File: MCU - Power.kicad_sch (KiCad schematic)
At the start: 29 parts, among them J3 B2B-PH-K-S, U1 STM32H743ZIT6TR

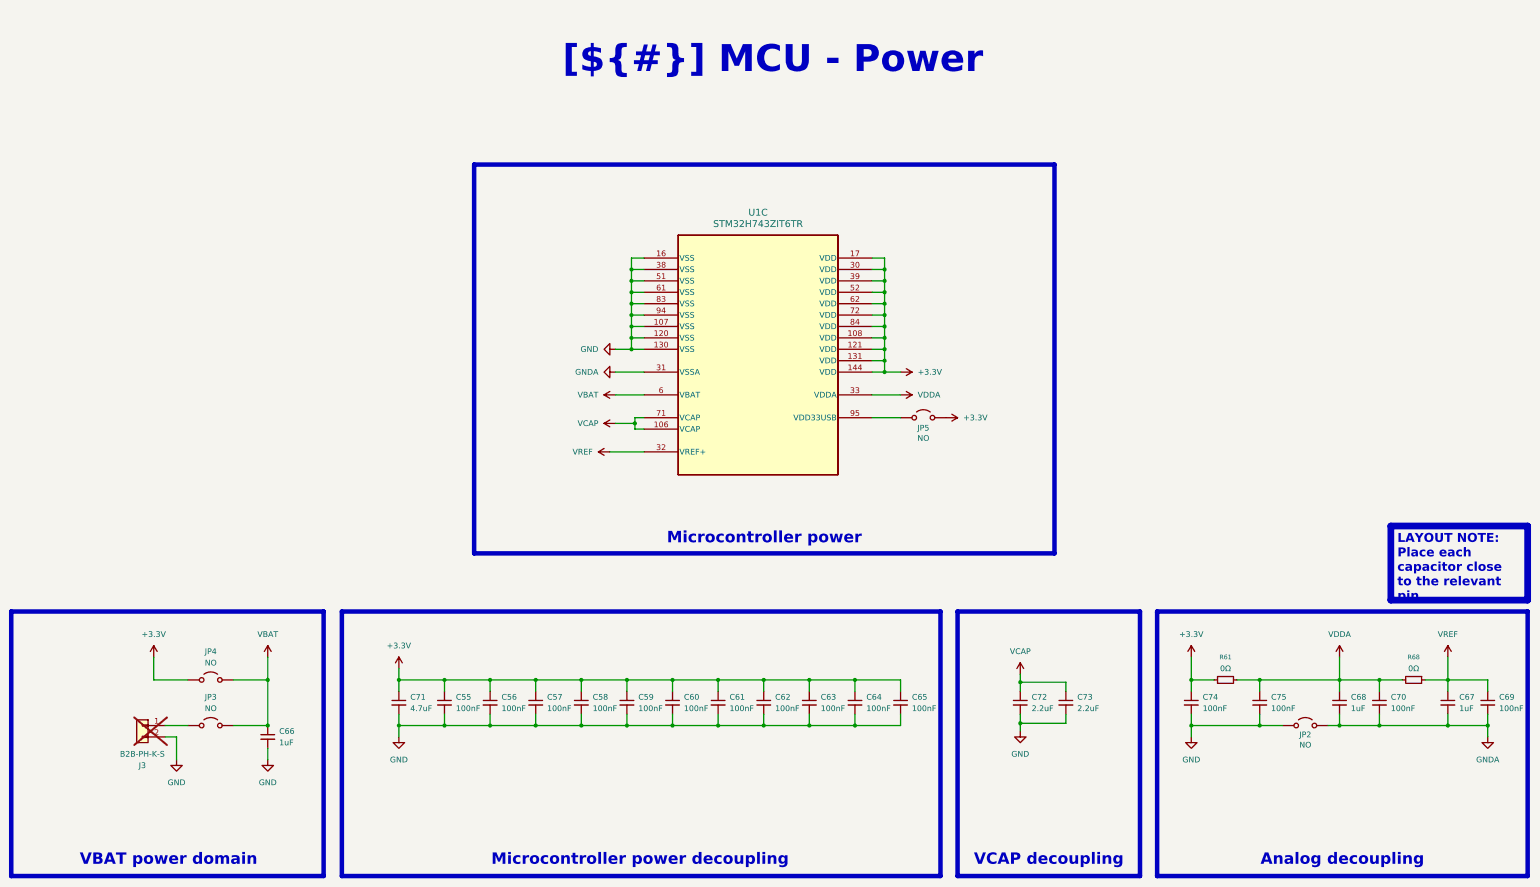
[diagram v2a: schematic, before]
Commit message: change some solder bridges from no to nc
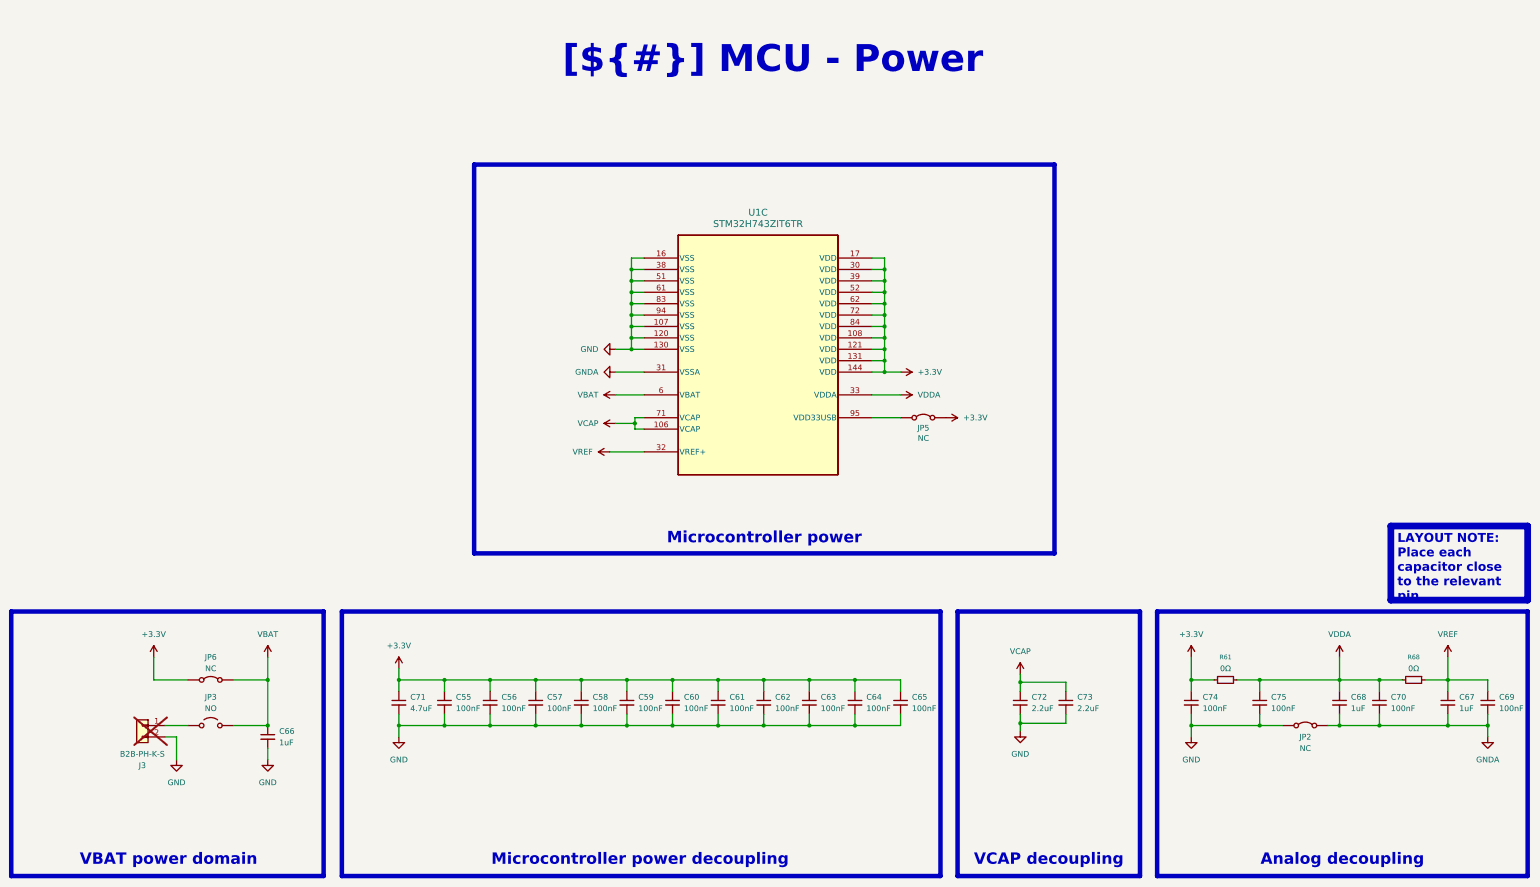
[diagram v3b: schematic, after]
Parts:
- removed JP2, JP4, JP5: NO, Jumper:SolderJumper-2_P1.3mm_Open_TrianglePad1.0x1.5mm, symbol 0_modules:Jumper_2_Open
- added JP2, JP5, JP6: NC, Jumper:SolderJumper-2_P1.3mm_Open_TrianglePad1.0x1.5mm, symbol 0_modules:Jumper_2_Bridged
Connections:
- net +3.3V: now also JP5.2 (B), JP6.1 (A)
- net GND: now also JP2.1 (A)
- net GNDA: now also JP2.2 (B)
- net VBAT: now also JP6.2 (B)
- net at U1.95 (VDD33USB): now also JP5.1 (A)
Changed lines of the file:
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@@
+	)
+	(symbol
+		(lib_id "0_modules:Jumper_2_Bridged")
+		(at 328.93 170.18 0)
+		(unit 1)
+		(exclude_from_sim no)
+		(in_bom yes)
+		(on_board yes)
+		(dnp no)
+		(property "Reference" "JP2"
+			(at 328.93 172.72 0)
+			(effects
+				(font
+					(size 1.27 1.27)
+				)
+			)
+		)
+		(property "Value" "NC"
+			(at 328.93 175.26 0)
+			(effects
+				(font
+					(size 1.27 1.27)
+				)
+			)
+		)
+		(property "Footprint" "Jumper:SolderJumper-2_P1.3mm_Open_TrianglePad1.0x1.5mm"
+			(at 328.93 170.18 0)
+			(effects
+				(font
+					(size 1.27 1.27)
+				)
+				(hide yes)
+			)
+		)
+		(property "Datasheet" "~"
+			(at 328.93 170.18 0)
+			(effects
+				(font
+					(size 1.27 1.27)
+				)
+				(hide yes)
+			)
+		)
+		(property "Description" "Jumper, 2-pole, closed/bridged"
+			(at 328.93 170.18 0)
+			(effects
+				(font
+					(size 1.27 1.27)
+				)
+				(hide yes)
+			)
+		)
+		(pin "1"
+		)
+		(pin "2"
+		)
+		(instances
+			(project "transmitter"
+				(path "/0650c7a8-acba-429c-9f8e-eec0baf0bc1c/fede4c36-00cc-4d3d-b71c-5243ba232202/7d5a1283-086b-46b0-8df7-a9850521fb5e"
+					(reference "JP2")
+					(unit 1)
+				)
+			)
+		)
 	)
 	(symbol
@@
 	)
 	(symbol
-		(lib_id "0_modules:Jumper_2_Open")
-		(at 328.93 170.18 0)
-		(unit 1)
-		(exclude_from_sim no)
-		(in_bom yes)
-		(on_board yes)
-		(dnp no)
-		(property "Reference" "JP2"
-			(at 328.93 172.212 0)
-			(effects
-				(font
-					(size 1.27 1.27)
-				)
-			)
-		)
-		(property "Value" "NO"
-			(at 328.93 174.498 0)
-			(effects
-				(font
-					(size 1.27 1.27)
-				)
-			)
-		)
-		(property "Footprint" "Jumper:SolderJumper-2_P1.3mm_Open_TrianglePad1.0x1.5mm"
-			(at 328.93 170.18 0)
-			(effects
-				(font
-					(size 1.27 1.27)
-				)
-				(hide yes)
-			)
-		)
-		(property "Datasheet" "~"
-			(at 328.93 170.18 0)
-			(effects
-				(font
-					(size 1.27 1.27)
-				)
-				(hide yes)
-			)
-		)
-		(property "Description" "Jumper, 2-pole, open"
-			(at 328.93 170.18 0)
-			(effects
-				(font
-					(size 1.27 1.27)
-				)
-				(hide yes)
-			)
-		)
-		(pin "1"
-		)
-		(pin "2"
-		)
-		(instances
-			(project "transmitter"
-				(path "/0650c7a8-acba-429c-9f8e-eec0baf0bc1c/fede4c36-00cc-4d3d-b71c-5243ba232202/7d5a1283-086b-46b0-8df7-a9850521fb5e"
-					(reference "JP2")
-					(unit 1)
-				)
-			)
-		)
-	)
-	(symbol
 		(lib_id "0_capacitors:CL05B104KO5NNNC")
 		(at 318.77 165.1 0)
@@
 	)
 	(symbol
+		(lib_id "0_modules:Jumper_2_Bridged")
+		(at 243.84 101.6 0)
+		(unit 1)
+		(exclude_from_sim no)
+		(in_bom yes)
+		(on_board yes)
+		(dnp no)
+		(property "Reference" "JP5"
+			(at 243.84 103.886 0)
+			(effects
+				(font
+					(size 1.27 1.27)
+				)
+			)
+		)
+		(property "Value" "NC"
+			(at 243.84 106.172 0)
+			(effects
+				(font
+					(size 1.27 1.27)
+				)
+			)
+		)
+		(property "Footprint" "Jumper:SolderJumper-2_P1.3mm_Open_TrianglePad1.0x1.5mm"
+			(at 243.84 101.6 0)
+			(effects
+				(font
+					(size 1.27 1.27)
+				)
+				(hide yes)
+			)
+		)
+		(property "Datasheet" "~"
+			(at 243.84 101.6 0)
+			(effects
+				(font
+					(size 1.27 1.27)
+				)
+				(hide yes)
+			)
+		)
+		(property "Description" "Jumper, 2-pole, closed/bridged"
+			(at 243.84 101.6 0)
+			(effects
+				(font
+					(size 1.27 1.27)
+				)
+				(hide yes)
+			)
+		)
+		(pin "1"
+		)
+		(pin "2"
+		)
+		(instances
+			(project ""
+				(path "/0650c7a8-acba-429c-9f8e-eec0baf0bc1c/fede4c36-00cc-4d3d-b71c-5243ba232202/7d5a1283-086b-46b0-8df7-a9850521fb5e"
+					(reference "JP5")
+					(unit 1)
+				)
+			)
+		)
+	)
+	(symbol
 		(lib_id "power:GND")
 		(at 127 172.72 0)
@@
 	)
 	(symbol
+		(lib_id "0_modules:Jumper_2_Bridged")
+		(at 85.09 160.02 0)
+		(unit 1)
+		(exclude_from_sim no)
+		(in_bom yes)
+		(on_board yes)
+		(dnp no)
+		(fields_autoplaced yes)
+		(property "Reference" "JP6"
+			(at 85.09 154.94 0)
+			(effects
+				(font
+					(size 1.27 1.27)
+				)
+			)
+		)
+		(property "Value" "NC"
+			(at 85.09 157.48 0)
+			(effects
+				(font
+					(size 1.27 1.27)
+				)
+			)
+		)
+		(property "Footprint" "Jumper:SolderJumper-2_P1.3mm_Open_TrianglePad1.0x1.5mm"
+			(at 85.09 160.02 0)
+			(effects
+				(font
+					(size 1.27 1.27)
+				)
+				(hide yes)
+			)
+		)
+		(property "Datasheet" "~"
+			(at 85.09 160.02 0)
+			(effects
+				(font
+					(size 1.27 1.27)
+				)
+				(hide yes)
+			)
+		)
+		(property "Description" "Jumper, 2-pole, closed/bridged"
+			(at 85.09 160.02 0)
+			(effects
+				(font
+					(size 1.27 1.27)
+				)
+				(hide yes)
+			)
+		)
+		(pin "1"
+		)
+		(pin "2"
+		)
+		(instances
+			(project "transmitter"
+				(path "/0650c7a8-acba-429c-9f8e-eec0baf0bc1c/fede4c36-00cc-4d3d-b71c-5243ba232202/7d5a1283-086b-46b0-8df7-a9850521fb5e"
+					(reference "JP6")
+					(unit 1)
+				)
+			)
+		)
+	)
+	(symbol
 		(lib_id "0_capacitors:CL05B104KO5NNNC")
 		(at 147.32 165.1 0)
@@
 	)
 	(symbol
-		(lib_id "0_modules:Jumper_2_Open")
-		(at 85.09 160.02 0)
-		(unit 1)
-		(exclude_from_sim no)
-		(in_bom yes)
-		(on_board yes)
-		(dnp no)
-		(fields_autoplaced yes)
-		(property "Reference" "JP4"
-			(at 85.09 153.67 0)
-			(effects
-				(font
-					(size 1.27 1.27)
-				)
-			)
-		)
-		(property "Value" "NO"
-			(at 85.09 156.21 0)
-			(effects
-				(font
-					(size 1.27 1.27)
-				)
-			)
-		)
-		(property "Footprint" "Jumper:SolderJumper-2_P1.3mm_Open_TrianglePad1.0x1.5mm"
-			(at 85.09 160.02 0)
-			(effects
-				(font
-					(size 1.27 1.27)
-				)
-				(hide yes)
-			)
-		)
-		(property "Datasheet" "~"
-			(at 85.09 160.02 0)
-			(effects
-				(font
-					(size 1.27 1.27)
-				)
-				(hide yes)
-			)
-		)
-		(property "Description" "Jumper, 2-pole, open"
-			(at 85.09 160.02 0)
-			(effects
-				(font
-					(size 1.27 1.27)
-				)
-				(hide yes)
-			)
-		)
-		(pin "1"
-		)
-		(pin "2"
-		)
-		(instances
-			(project "transmitter"
-				(path "/0650c7a8-acba-429c-9f8e-eec0baf0bc1c/fede4c36-00cc-4d3d-b71c-5243ba232202/7d5a1283-086b-46b0-8df7-a9850521fb5e"
-					(reference "JP4")
-					(unit 1)
-				)
-			)
-		)
-	)
-	(symbol
 		(lib_id "power:VDDA")
 		(at 336.55 154.94 0)
@@
 					(unit 1)
 				)
-			)
-		)
-	)
-	(symbol
-		(lib_id "0_modules:Jumper_2_Open")
-		(at 243.84 101.6 0)
-		(unit 1)
-		(exclude_from_sim no)
-		(in_bom yes)
-		(on_board yes)
-		(dnp no)
-		(property "Reference" "JP5"
-			(at 243.84 103.886 0)
-			(effects
-				(font
-					(size 1.27 1.27)
-				)
-			)
-		)
-		(property "Value" "NO"
-			(at 243.84 106.172 0)
-			(effects
-				(font
-					(size 1.27 1.27)
-				)
-			)
-		)
-		(property "Footprint" "Jumper:SolderJumper-2_P1.3mm_Open_TrianglePad1.0x1.5mm"
-			(at 243.84 101.6 0)
-			(effects
-				(font
-					(size 1.27 1.27)
-				)
-				(hide yes)
-			)
-		)
-		(property "Datasheet" "~"
-			(at 243.84 101.6 0)
-			(effects
-				(font
-					(size 1.27 1.27)
-				)
-				(hide yes)
-			)
-		)
-		(property "Description" "Jumper, 2-pole, open"
-			(at 243.84 101.6 0)
-			(effects
-				(font
-					(size 1.27 1.27)
-				)
-				(hide yes)
-			)
-		)
-		(pin "1"
-		)
-		(pin "2"
-		)
-		(instances
-			(project "transmitter"
-				(path "/0650c7a8-acba-429c-9f8e-eec0baf0bc1c/fede4c36-00cc-4d3d-b71c-5243ba232202/7d5a1283-086b-46b0-8df7-a9850521fb5e"
-					(reference "JP5")
-					(unit 1)
-				)

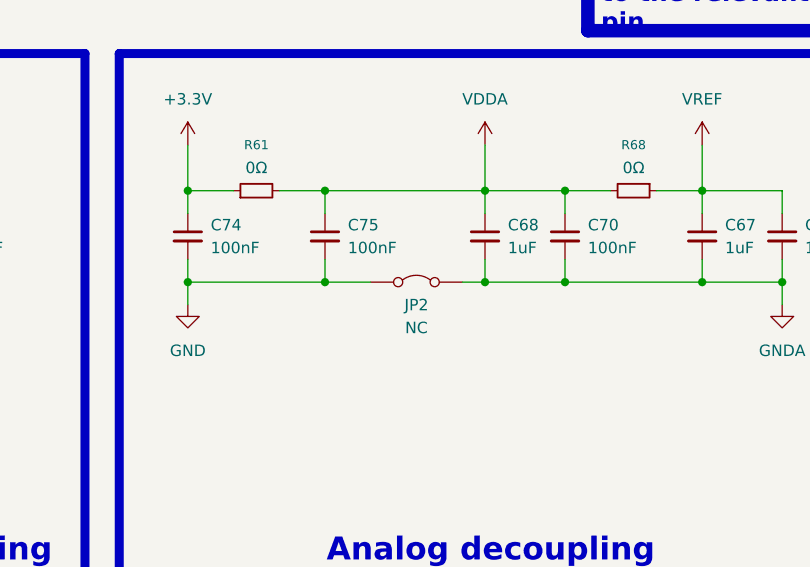
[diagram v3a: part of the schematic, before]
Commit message: added some small changes on schematics - added some decoupling caps and test production files
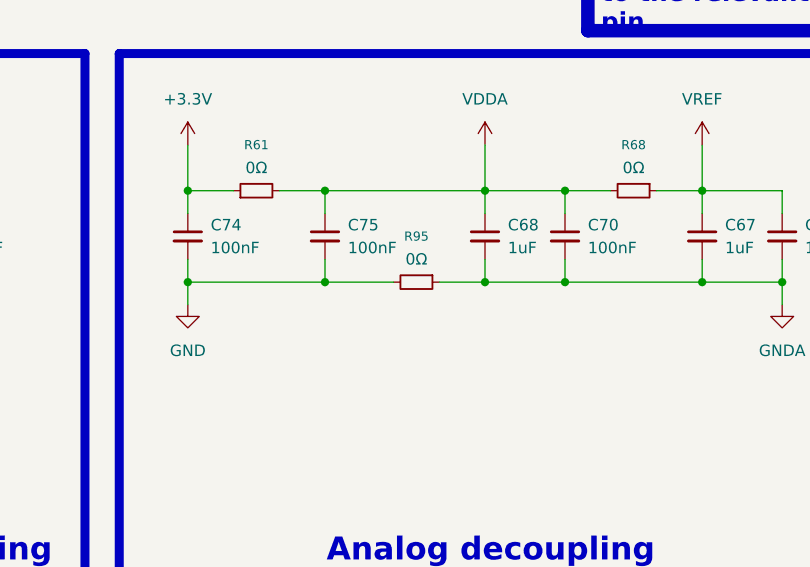
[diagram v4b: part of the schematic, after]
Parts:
- removed JP2: NC, Jumper:SolderJumper-2_P1.3mm_Open_TrianglePad1.0x1.5mm, symbol 0_modules:Jumper_2_Bridged
- added R95: 0Ω, 0_resistors:R_0402_1005Metric, symbol 0_resistors:0402WGF0000TCE
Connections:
- net GND: now also R95.2
- net GNDA: now also R95.1
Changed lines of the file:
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@@
 	(wire
 		(pts
-			(xy 318.77 170.18) (xy 323.85 170.18)
+			(xy 331.47 170.18) (xy 336.55 170.18)
+		)
+		(stroke
+			(width 0)
+			(type default)
+		)
+	)
+	(wire
+		(pts
+			(xy 318.77 170.18) (xy 326.39 170.18)
 		)
 		(stroke
@@
 	(wire
 		(pts
-			(xy 334.01 170.18) (xy 336.55 170.18)
-		)
-		(stroke
-			(width 0)
-			(type default)
-		)
-	)
-	(wire
-		(pts
 			(xy 232.41 101.6) (xy 238.76 101.6)
 		)
@@
 	)
 	(symbol
-		(lib_id "0_modules:Jumper_2_Bridged")
-		(at 328.93 170.18 0)
-		(unit 1)
-		(exclude_from_sim no)
-		(in_bom yes)
-		(on_board yes)
-		(dnp no)
-		(property "Reference" "JP2"
-			(at 328.93 172.72 0)
-			(effects
-				(font
-					(size 1.27 1.27)
-				)
-			)
-		)
-		(property "Value" "NC"
-			(at 328.93 175.26 0)
-			(effects
-				(font
-					(size 1.27 1.27)
-				)
-			)
-		)
-		(property "Footprint" "Jumper:SolderJumper-2_P1.3mm_Open_TrianglePad1.0x1.5mm"
-			(at 328.93 170.18 0)
-			(effects
-				(font
-					(size 1.27 1.27)
-				)
-				(hide yes)
-			)
-		)
-		(property "Datasheet" "~"
-			(at 328.93 170.18 0)
-			(effects
-				(font
-					(size 1.27 1.27)
-				)
-				(hide yes)
-			)
-		)
-		(property "Description" "Jumper, 2-pole, closed/bridged"
-			(at 328.93 170.18 0)
-			(effects
-				(font
-					(size 1.27 1.27)
-				)
-				(hide yes)
-			)
-		)
-		(pin "1"
-		)
-		(pin "2"
-		)
-		(instances
-			(project "transmitter"
-				(path "/0650c7a8-acba-429c-9f8e-eec0baf0bc1c/fede4c36-00cc-4d3d-b71c-5243ba232202/7d5a1283-086b-46b0-8df7-a9850521fb5e"
-					(reference "JP2")
-					(unit 1)
-				)
-			)
-		)
-	)
-	(symbol
 		(lib_id "0_capacitors:CL05B104KO5NNNC")
 		(at 157.48 165.1 0)
@@
 					(unit 1)
 				)
+			)
+		)
+	)
+	(symbol
+		(lib_id "0_resistors:0402WGF0000TCE")
+		(at 328.93 170.18 270)
+		(unit 1)
+		(exclude_from_sim no)
+		(in_bom yes)
+		(on_board yes)
+		(dnp no)
+		(fields_autoplaced yes)
+		(property "Reference" "R95"
+			(at 328.93 165.1 90)
+			(effects
+				(font
+					(size 1.016 1.016)
+				)
+			)
+		)
+		(property "Value" "0Ω"
+			(at 328.93 167.64 90)
+			(effects
+				(font
+					(size 1.27 1.27)
+				)
+			)
+		)
+		(property "Footprint" "0_resistors:R_0402_1005Metric"
+			(at 328.93 170.18 0)
+			(effects
+				(font
+					(size 1.27 1.27)
+				)
+				(hide yes)
+			)
+		)
+		(property "Datasheet" "~"
+			(at 328.93 170.18 0)
+			(effects
+				(font
+					(size 1.27 1.27)
+				)
+				(hide yes)
+			)
+		)
+		(property "Description" "50V ±800ppm/℃ ±1% 0Ω 0402"
+			(at 328.93 170.18 0)
+			(effects
+				(font
+					(size 1.27 1.27)
+				)
+				(hide yes)
+			)
+		)
+		(property "Supplier 1" "JLCPCB"
+			(at 328.93 170.18 0)
+			(effects
+				(font
+					(size 1.27 1.27)
+				)
+				(hide yes)
+			)
+		)
+		(property "Supplier Part Number 1" "C17168"
+			(at 328.93 170.18 0)
+			(effects
+				(font
+					(size 1.27 1.27)
+				)
+				(hide yes)
+			)
+		)
+		(pin "2"
+		)
+		(pin "1"
+		)
+		(instances
+			(project "transmitter"
+				(path "/0650c7a8-acba-429c-9f8e-eec0baf0bc1c/fede4c36-00cc-4d3d-b71c-5243ba232202/7d5a1283-086b-46b0-8df7-a9850521fb5e"
+					(reference "R95")
+					(unit 1)
+				)

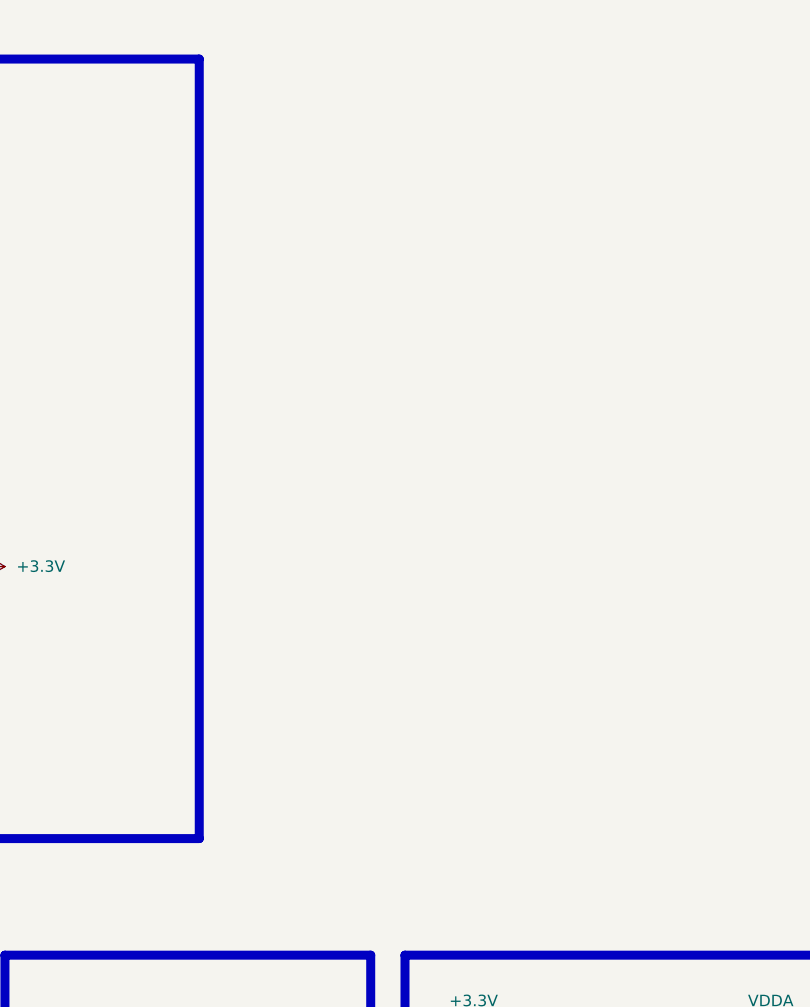
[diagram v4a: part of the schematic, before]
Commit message: added fiducal markers, mounting holes, testpoints
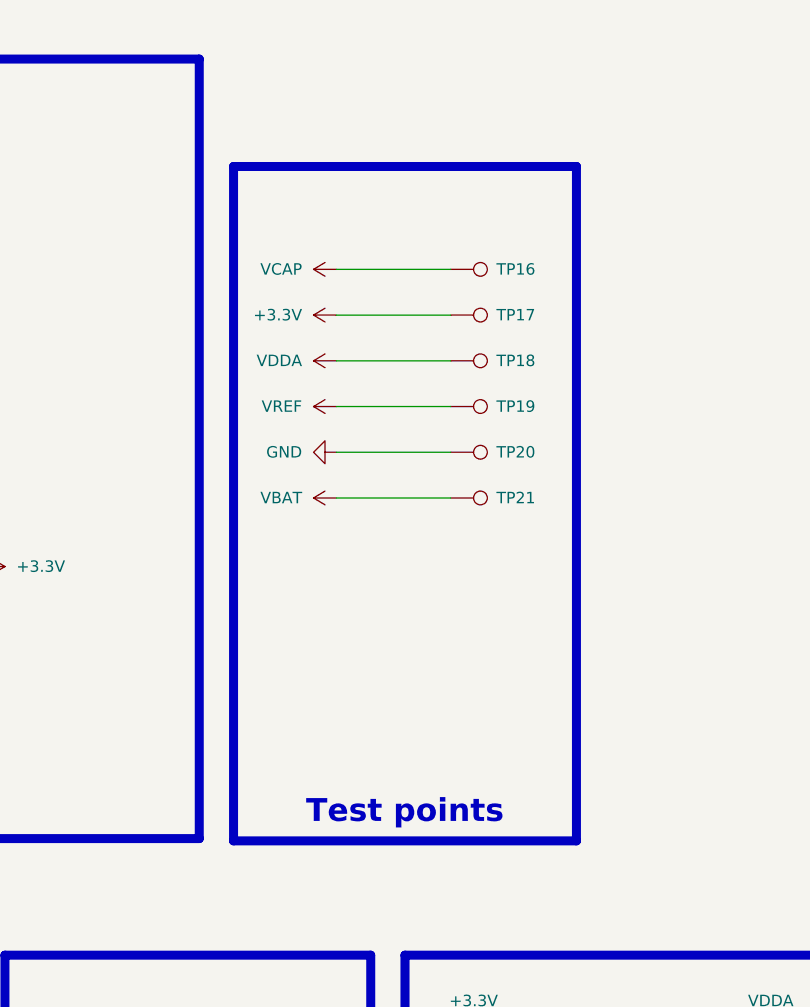
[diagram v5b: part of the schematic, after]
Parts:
- added TP16, TP17, TP18, TP19, TP20, TP21: TestPoint, 0_pads:TestPoint_Pad_D0.4mm_Back, symbol Connector:TestPoint
- U1: footprint LQFP-144_1_STM -> (none)
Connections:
- net +3.3V: now also TP17.1
- net GND: now also TP20.1
- net VBAT: now also TP21.1
- net VCAP: now also TP16.1
- net VDDA: now also TP18.1
- net VREF: now also TP19.1

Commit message: some visual changes, color of nets etc
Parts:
- U1: footprint (none) -> 0_integrated_circuits:LQFP-144_1_STM
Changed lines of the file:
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@@
 			)
 		)
-		(property "Footprint" ""
+		(property "Footprint" "0_integrated_circuits:LQFP-144_1_STM"
 			(at 181.61 66.04 0)
 			(effects
